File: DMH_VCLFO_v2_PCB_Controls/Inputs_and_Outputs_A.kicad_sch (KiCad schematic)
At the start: 40 parts, among them J1 TS_Jack_6.35mm_Sw, J19 Conn_01x08, J2 TS_Jack_6.35mm_Sw, J20 Conn_01x08, J22 Conn_01x08, J23 Conn_01x08, J3 TS_Jack_6.35mm_Sw, J4 TS_Jack_6.35mm_Sw, J5 TS_Jack_6.35mm_Sw, J6 TS_Jack_6.35mm_Sw, Q1 BC548, Q2 BC558, SW1 SW_SPDT, SW2 SPDT_OnOffOn, SW3 SW_SPDT, SW4 SW_SPDT, U1 TL074

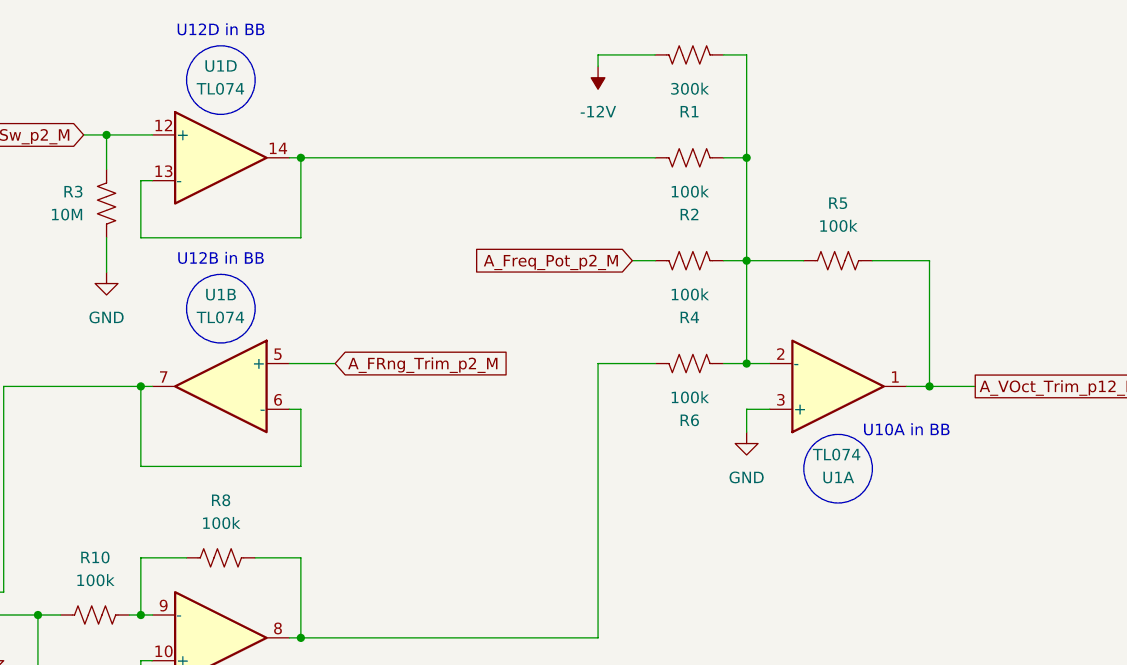
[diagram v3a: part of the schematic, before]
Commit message: Added project with Single VCLFO schematic
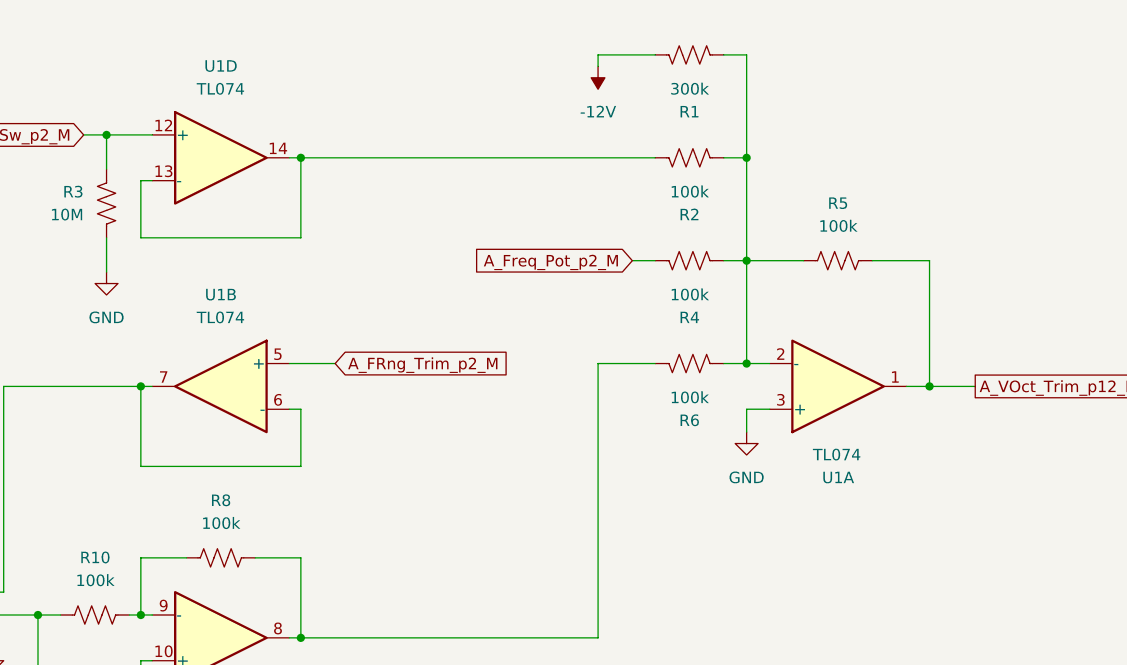
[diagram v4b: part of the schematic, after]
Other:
- note removed: "U10A in BB"
- note removed: "U12B in BB"
- note removed: "U12D in BB"
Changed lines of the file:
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@@
 		(comment 1 "PCB for 10cm Kosmo format synthesizer module")
-	)
-	(circle
-		(center 236.22 66.294)
-		(radius 3.81)
-		(stroke
-			(width 0)
-			(type default)
-		)
-		(fill
-			(type none)
-		)
-	)
-	(circle
-		(center 167.64 48.514)
-		(radius 3.81)
-		(stroke
-			(width 0)
-			(type default)
-		)
-		(fill
-			(type none)
-		)
-	)
-	(circle
-		(center 167.64 23.114)
-		(radius 3.81)
-		(stroke
-			(width 0)
-			(type default)
-		)
-		(fill
-			(type none)
-		)
-	)
-	(text "U12B in BB"
-		(exclude_from_sim no)
-		(at 167.64 43.18 0)
-		(effects
-			(font
-				(size 1.27 1.27)
-			)
-		)
-	)
-	(text "U10A in BB"
-		(exclude_from_sim no)
-		(at 243.84 62.23 0)
-		(effects
-			(font
-				(size 1.27 1.27)
-			)
-		)
-	)
-	(text "U12D in BB"
-		(exclude_from_sim no)
-		(at 167.64 17.78 0)
-		(effects
-			(font
-				(size 1.27 1.27)
-			)
-		)
 	)
 	(junction
